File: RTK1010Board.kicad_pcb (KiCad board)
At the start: 2 copper layers, 56.2 x 53.3 mm, 74 parts, among them J1 SMA, J2 IPEX, J3 USB_OTG, J4 BNO055, U1 RTK-1010, U2 MCP1700-3002E_SOT23, U3 MCP1700-3002E_SOT23, U4 ESP32-S2-WROVER

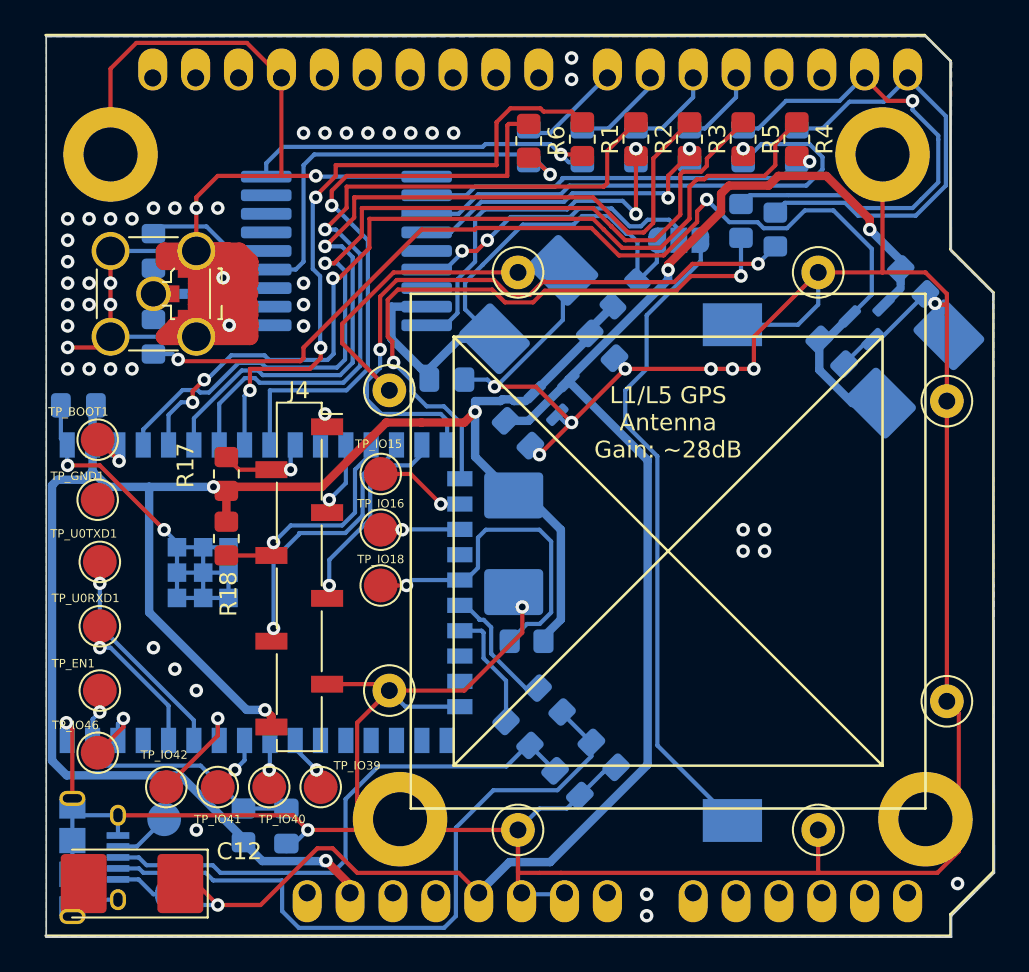
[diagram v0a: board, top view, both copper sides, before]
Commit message: LDO replaced by 500ma type
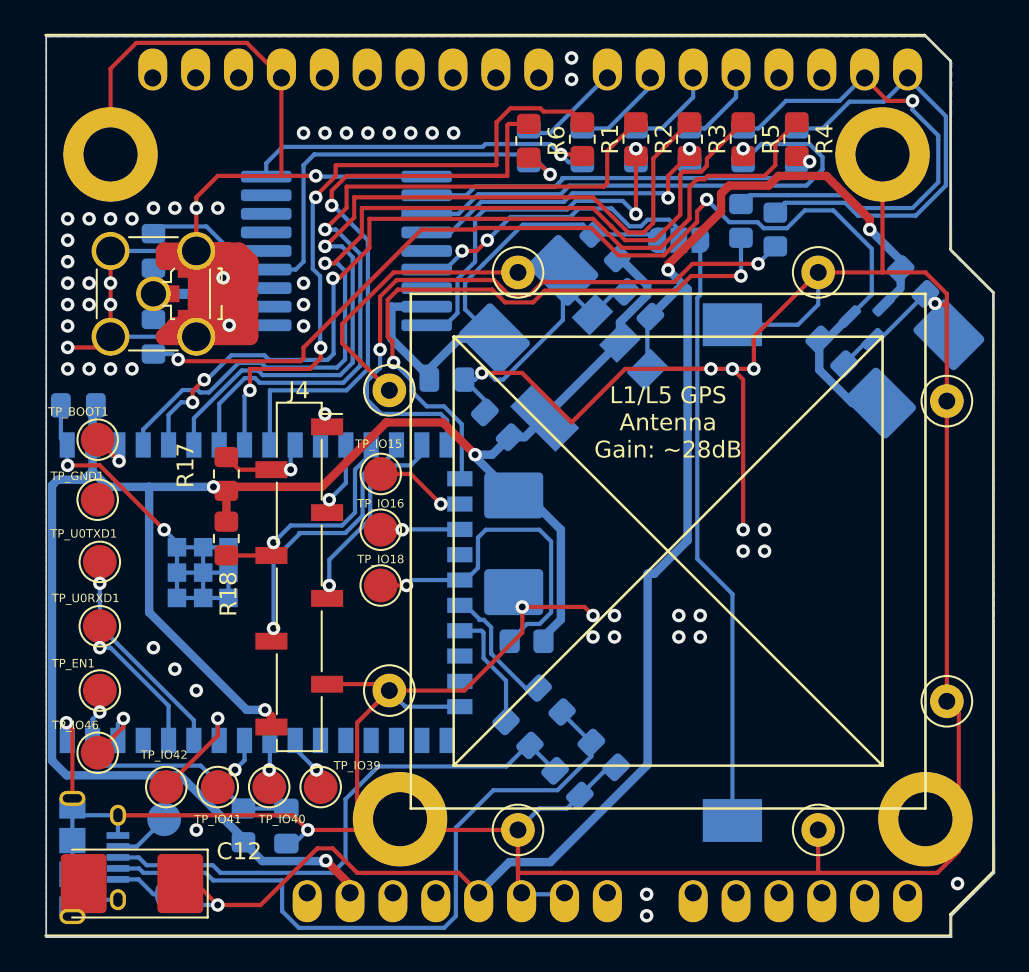
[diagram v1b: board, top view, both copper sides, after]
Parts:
- U2: value MCP1700-3002E_SOT23 -> NCP1117-3.3_SOT223; footprint Package_TO_SOT_SMD:SOT-23 -> Package_TO_SOT_SMD:SOT-223-3_TabPin2
- U3: value MCP1700-3002E_SOT23 -> MCP1700-3302E_SOT23
- moved C1 10.4 mm to (206.5, 89.5), turned to 135 degrees
- moved C4 7.77 mm to (198.2, 96.7), turned to 135 degrees
- moved L3 3.04 mm to (204.5, 86.1), turned to 135 degrees
- moved U2 1.66 mm to (203.2, 94.0), turned to -135 degrees
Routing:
- net GND: track 404.1 -> 425.5 mm, vias 62 -> 67
- net +3V3: track 118.4 -> 123.5 mm
- net Net-(C13-Pad1): track 34.2 -> 29.6 mm
- net Net-(BT1-Pad1): track 38.8 -> 35.3 mm
- net U5: track 96.5 -> 95.2 mm

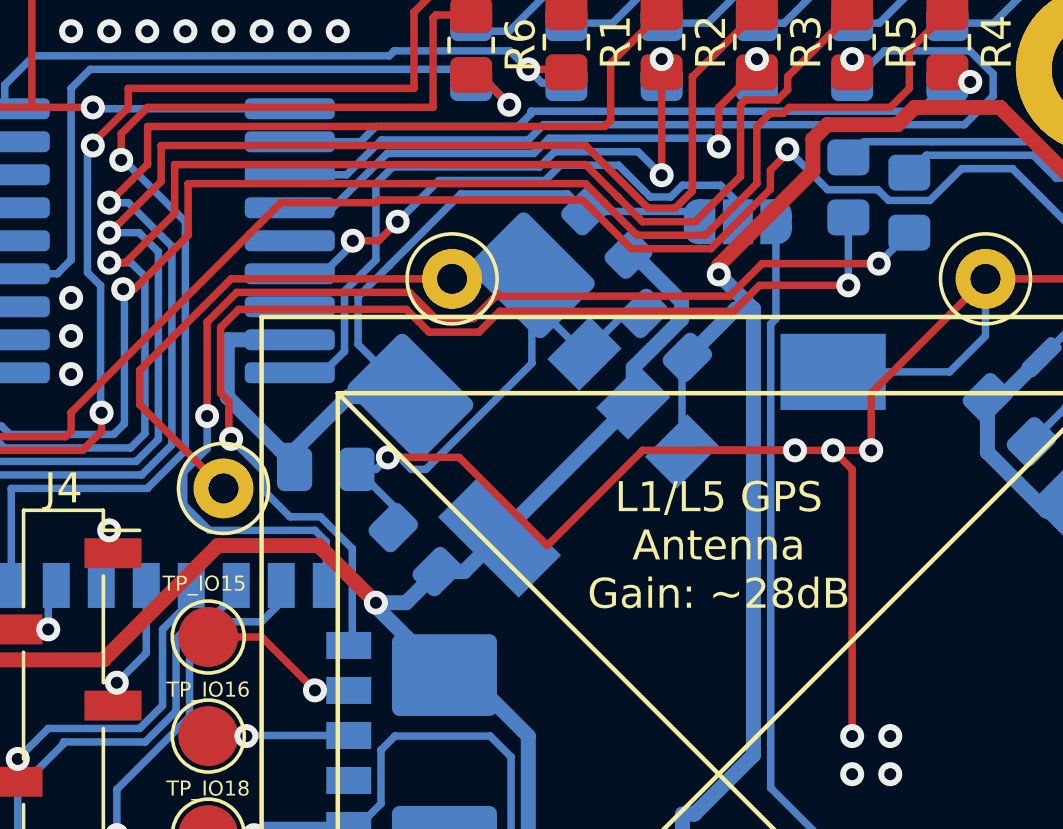
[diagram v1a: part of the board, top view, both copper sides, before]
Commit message: support for teseo-liv3fl added
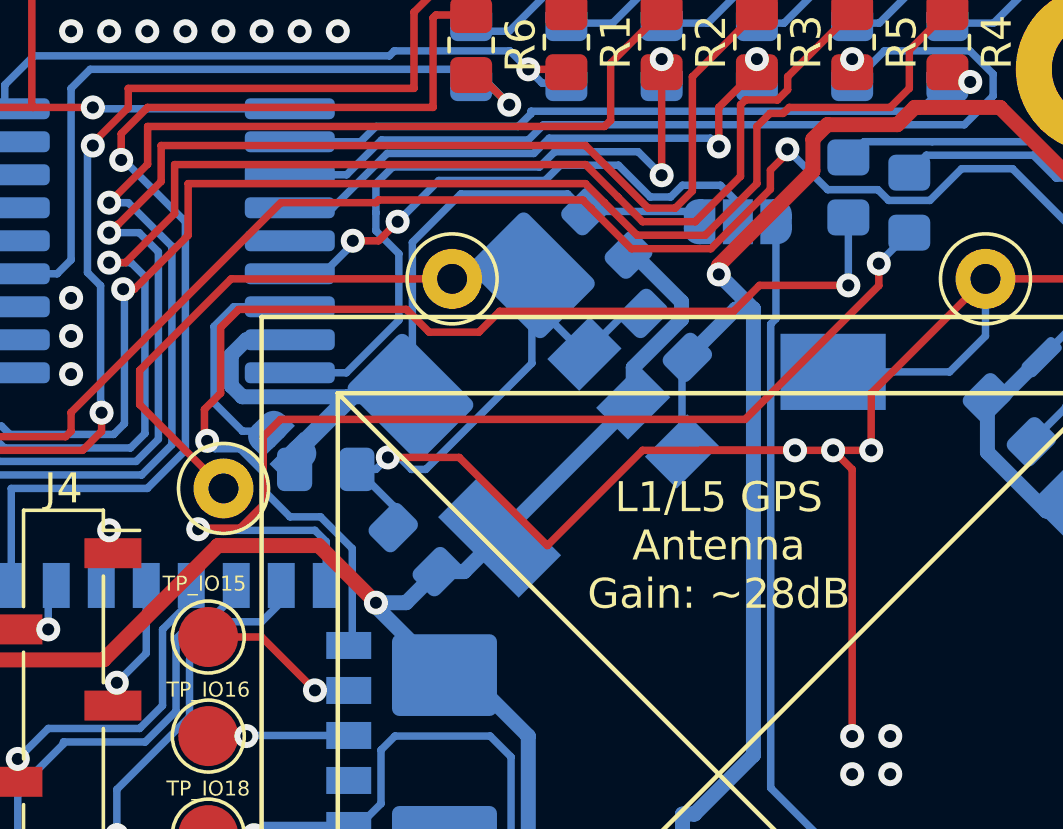
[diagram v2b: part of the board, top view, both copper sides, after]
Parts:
- added JP3: VCC_IO, Jumper:SolderJumper-2_P1.3mm_Open_RoundedPad1.0x1.5mm, B.Cu at (193.7, 93.2)
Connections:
- U1 pad 7: unconnected-(U1-Pad7) -> Net-(U1-Pad7)
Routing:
- net Net-(U1-Pad7): track 0.00 -> 7.55 mm
- net Net-(R19-Pad1): track 38.6 -> 35.5 mm
- net Net-(C13-Pad1): track 29.6 -> 30.9 mm
- net _EN: track 23.1 -> 24.2 mm
- net Net-(R20-Pad1): track 37.5 -> 38.4 mm

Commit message: ibom added
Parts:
- L3: value ?H -> 1.2uH
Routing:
- net GND: track 425.5 -> 423.4 mm, vias 67 -> 68
- net Net-(R20-Pad1): track 38.4 -> 37.5 mm
- net Net-(R5-Pad1): track 54.0 -> 54.6 mm
- net Net-(R6-Pad1): track 36.1 -> 35.5 mm
- net Net-(R1-Pad1): track 39.1 -> 38.5 mm
- net Net-(JP3-Pad2): track 7.55 -> 6.98 mm

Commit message: ibom updated
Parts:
- C2, C3: value 100nF -> 100pF
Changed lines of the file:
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@@
     (property "Sheetfile" "RTK1010Board.kicad_sch")
     (property "Sheetname" "")
-    (property "Variant" "B")
+    (property "Variant" "VarB")
     (attr smd)
     (fp_text reference "C12" (at -6.35 1.905) (layer "F.SilkS")
@@
     (property "Sheetfile" "RTK1010Board.kicad_sch")
     (property "Sheetname" "")
-    (property "Variant" "A,B")
+    (property "Variant" "VarA,VarB")
     (attr smd)
     (fp_text reference "J2" (at 5.08 1.905) (layer "F.SilkS") hide
@@
     (property "Sheetfile" "RTK1010Board.kicad_sch")
     (property "Sheetname" "")
-    (property "Variant" "B")
+    (property "Variant" "VarB")
     (attr smd)
     (fp_text reference "R5" (at 0 -1.65 90) (layer "F.SilkS")
@@
     (property "Sheetfile" "RTK1010Board.kicad_sch")
     (property "Sheetname" "")
-    (property "Variant" "A")
+    (property "Variant" "VarA")
     (attr through_hole)
     (fp_text reference "XA1" (at 7.62 -54.61) (layer "F.SilkS") hide
@@
     (property "Sheetfile" "RTK1010Board.kicad_sch")
     (property "Sheetname" "")
-    (property "Variant" "B")
+    (property "Variant" "VarB")
     (attr smd)
     (fp_text reference "R4" (at 0 -1.65 90) (layer "F.SilkS")
@@
     (property "Sheetfile" "RTK1010Board.kicad_sch")
     (property "Sheetname" "")
+    (property "Variant" "VarB")
     (attr smd)
     (fp_text reference "U4" (at 2.62 2.235 180) (layer "B.SilkS")
@@
     (property "Sheetfile" "RTK1010Board.kicad_sch")
     (property "Sheetname" "")
-    (property "Variant" "")
+    (property "Variant" "VarB")
     (attr smd)
     (fp_text reference "C3" (at -3.02795 0.011857 135) (layer "B.SilkS")
       (effects (font (size 1 1) (thickness 0.15)) (justify mirror))
     )
-    (fp_text value "100nF" (at 0 -1.68 135) (layer "B.Fab")
+    (fp_text value "100pF" (at 0 -1.68 135) (layer "B.Fab")
       (effects (font (size 1 1) (thickness 0.15)) (justify mirror))
     )
@@
     (property "Sheetfile" "RTK1010Board.kicad_sch")
     (property "Sheetname" "")
+    (property "Variant" "VarB")
     (attr smd)
     (fp_text reference "C11" (at 0 -0.254 135) (layer "B.SilkS")
@@
     (property "Sheetfile" "RTK1010Board.kicad_sch")
     (property "Sheetname" "")
-    (property "Variant" "A,B")
+    (property "Variant" "VarA,VarB")
     (attr smd)
     (fp_text reference "C5" (at 0 1.68) (layer "B.SilkS")
@@
     (property "Sheetfile" "RTK1010Board.kicad_sch")
     (property "Sheetname" "")
-    (property "Variant" "A")
+    (property "Variant" "VarA")
     (attr smd)
     (fp_text reference "R8" (at 2 1.27 180) (layer "B.SilkS")
@@
     (property "Sheetfile" "RTK1010Board.kicad_sch")
     (property "Sheetname" "")
-    (property "Variant" "B")
+    (property "Variant" "VarB")
     (attr smd)
     (fp_text reference "C2" (at -2.694077 0 135) (layer "B.SilkS")
       (effects (font (size 1 1) (thickness 0.15)) (justify mirror))
     )
-    (fp_text value "100nF" (at 0 -1.68 135) (layer "B.Fab")
+    (fp_text value "100pF" (at 0 -1.68 135) (layer "B.Fab")
       (effects (font (size 1 1) (thickness 0.15)) (justify mirror))
     )
@@
     (property "Sheetfile" "RTK1010Board.kicad_sch")
     (property "Sheetname" "")
-    (property "Variant" "A,B")
+    (property "Variant" "VarA,VarB")
     (attr smd)
     (fp_text reference "U1" (at 5.08 2.54 unlocked) (layer "B.Cu") hide
@@
     (property "Sheetfile" "RTK1010Board.kicad_sch")
     (property "Sheetname" "")
-    (property "Variant" "B")
+    (property "Variant" "VarB")
     (attr smd)
     (fp_text reference "R13" (at 0.449013 -4.041115 135) (layer "B.SilkS")
@@
     (property "Sheetfile" "RTK1010Board.kicad_sch")
     (property "Sheetname" "")
-    (property "Variant" "B")
+    (property "Variant" "VarB")
     (attr smd)
     (fp_text reference "R15" (at 2.81 -0.381) (layer "B.SilkS")
@@
     (property "Sheetfile" "RTK1010Board.kicad_sch")
     (property "Sheetname" "")
+    (property "Variant" "VarB")
     (attr smd)
     (fp_text reference "C4" (at 0 1.68 135) (layer "B.SilkS")
@@
     (property "Sheetfile" "RTK1010Board.kicad_sch")
     (property "Sheetname" "")
-    (property "Variant" "B")
+    (property "Variant" "VarB")
     (attr smd)
     (fp_text reference "C8" (at 0 1.68) (layer "B.SilkS")
@@
     (property "Sheetfile" "RTK1010Board.kicad_sch")
     (property "Sheetname" "")
+    (property "Variant" "VarB")
     (attr smd)
     (fp_text reference "C1" (at 0 1.68 135) (layer "B.SilkS")
@@
     (property "Sheetfile" "RTK1010Board.kicad_sch")
     (property "Sheetname" "")
-    (property "Variant" "A,B")
+    (property "Variant" "VarA,VarB")
     (attr smd)
     (fp_text reference "C13" (at 0 2.7 45) (layer "B.SilkS")
@@
     (property "Sheetfile" "RTK1010Board.kicad_sch")
     (property "Sheetname" "")
-    (property "Variant" "B")
+    (property "Variant" "VarB")
     (attr smd)
     (fp_text reference "C9" (at -0.2325 1.651 180) (layer "B.SilkS")
@@
     (property "Sheetfile" "RTK1010Board.kicad_sch")
     (property "Sheetname" "")
-    (property "Variant" "B")
+    (property "Variant" "VarB")
     (attr smd)
     (fp_text reference "R16" (at 1.143 -1.651) (layer "B.SilkS")
@@
     (property "Sheetfile" "RTK1010Board.kicad_sch")
     (property "Sheetname" "")
-    (property "Variant" "B")
+    (property "Variant" "VarB")
     (attr smd)
     (fp_text reference "R14" (at 0 1.65 135) (layer "B.SilkS")
@@
     (property "Sheetfile" "RTK1010Board.kicad_sch")
     (property "Sheetname" "")
-    (property "Variant" "A,B")
+    (property "Variant" "VarA,VarB")
     (attr smd)
     (fp_text reference "L1" (at -2.54 -0.635 90) (layer "B.SilkS")
@@
     (property "Sheetfile" "RTK1010Board.kicad_sch")
     (property "Sheetname" "")
-    (property "Variant" "B")
+    (property "Variant" "VarB")
     (attr smd)
     (fp_text reference "J3" (at -3.76 0.67) (layer "B.SilkS")
@@
     (property "Sheetfile" "RTK1010Board.kicad_sch")
     (property "Sheetname" "")
+    (property "Variant" "VarB")
     (attr smd)
     (fp_text reference "U2" (at 0 4.5 45) (layer "B.SilkS")
@@
     (property "Sheetfile" "RTK1010Board.kicad_sch")
     (property "Sheetname" "")
-    (property "Variant" "A")
+    (property "Variant" "VarA")
     (attr smd)
     (fp_text reference "R7" (at -2 -1.905 180) (layer "B.SilkS")

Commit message: V1.0
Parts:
- added J5: Conn_GPS, footprints:CONN-TE-MICROMATCH-4X2-SMD, F.Cu at (179.4, 107.3)
- added TP_IO1: TestPoint, TestPoint:TestPoint_Pad_D2.0mm, F.Cu at (178.6, 114.9)
- added TP_IO17: TestPoint, TestPoint:TestPoint_Pad_D2.0mm, F.Cu at (194.9, 99.7)
- added TP_IO21: TestPoint, TestPoint:TestPoint_Pad_D2.0mm, F.Cu at (194.9, 106.0)
- added TP_IO26: TestPoint, TestPoint:TestPoint_Pad_D2.0mm, F.Cu at (194.9, 102.9)
- moved R18 4.91 mm to (181.4, 98.5), turned to 0 degrees
- moved R17 3.08 mm to (181.4, 96.6), turned to 0 degrees
- moved TP_EN1 0.63 mm to (174.0, 112.4)
- moved TP_U0RXD1 0.63 mm to (174.0, 108.6)
- moved TP_U0TXD1 0.63 mm to (174.0, 104.8)
- moved TP_BOOT1 0.51 mm to (174.0, 97.5)
- moved TP_GND1 0.51 mm to (174.0, 101.1)
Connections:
- U4 pad 27: unconnected-(U4-Pad27) -> GPS_RXD
- U4 pad 28: unconnected-(U4-Pad28) -> GPS_SCL
- U4 pad 29: unconnected-(U4-Pad29) -> GPS_TXD
- U4 pad 30: unconnected-(U4-Pad30) -> GPS_SDA
- U4 pad 31: unconnected-(U4-Pad31) -> GPS_7
- U4 pad 32: unconnected-(U4-Pad32) -> GPS_8
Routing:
- net GPS_RXD: track 0.00 -> 29.2 mm, vias 0 -> 1
- net GPS_TXD: track 0.00 -> 27.8 mm, vias 0 -> 1
- net GPS_SCL: track 0.00 -> 23.5 mm, vias 0 -> 1
- net GPS_SDA: track 0.00 -> 23.1 mm, vias 0 -> 1
- net GPS_7: track 0.00 -> 15.7 mm, vias 0 -> 1
- net GND: track 423.4 -> 436.1 mm, vias 68 -> 75
- net unconnected-(U4-Pad25): track 0.00 -> 12.1 mm, vias 0 -> 1
- net unconnected-(U4-Pad20): track 0.00 -> 10.7 mm, vias 0 -> 1
- net GPS_8: track 0.00 -> 9.24 mm, vias 0 -> 1
- net +3V3: track 123.5 -> 130.6 mm, vias 4 -> 5
- net unconnected-(U4-Pad24): track 0.00 -> 5.54 mm, vias 0 -> 1
- net BNO_ADDR: track 13.4 -> 16.4 mm, vias 1 -> 2
- net unconnected-(U4-Pad39): track 0.00 -> 2.41 mm, vias 0 -> 1
- net Net-(R19-Pad1): track 35.5 -> 37.1 mm
- net Net-(R5-Pad1): track 54.6 -> 53.0 mm
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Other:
- board text added: "RTK-1010 Board V1.0"
